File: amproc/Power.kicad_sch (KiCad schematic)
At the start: 42 parts

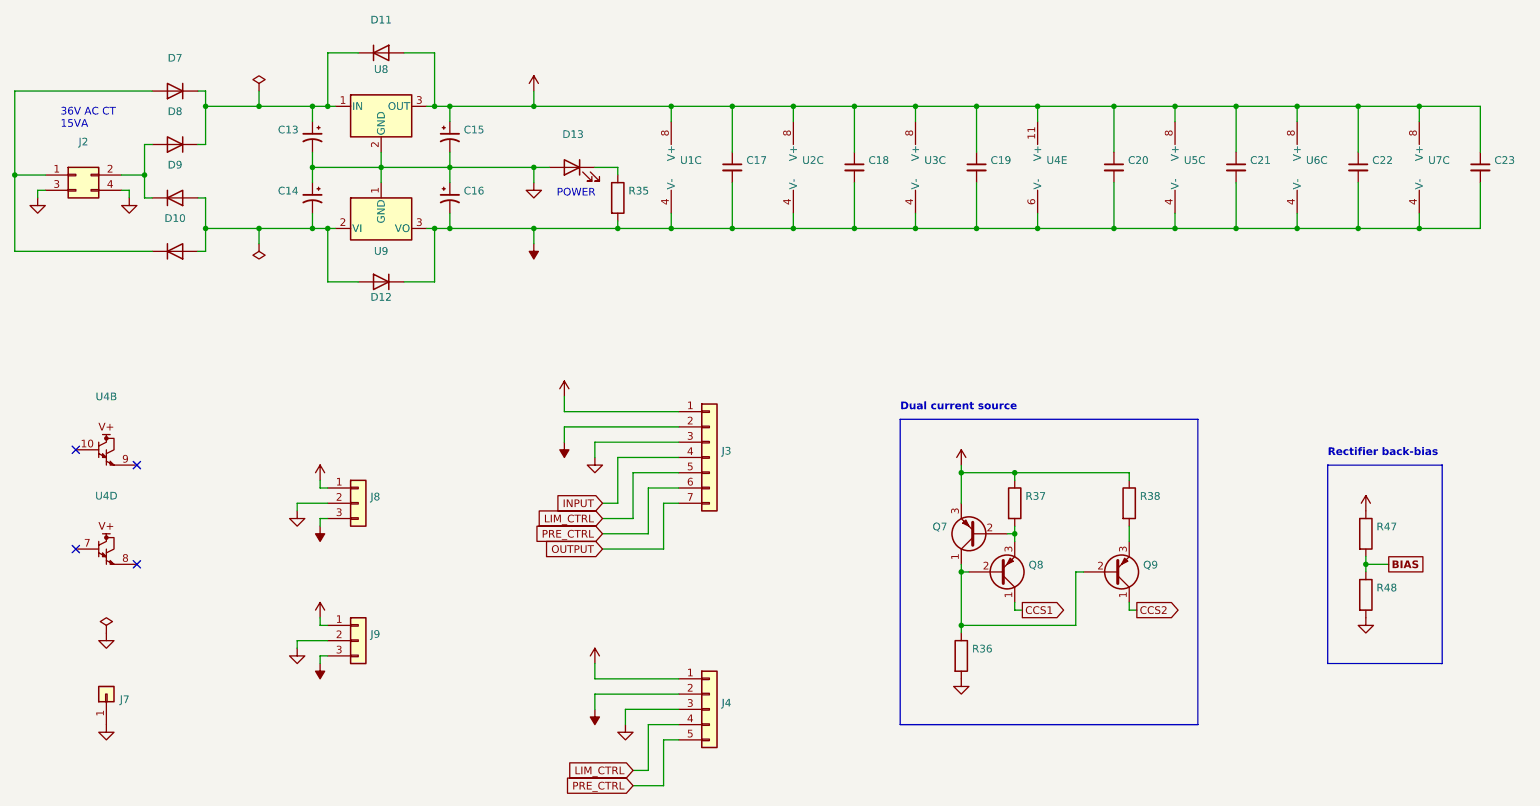
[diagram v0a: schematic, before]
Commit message: Fix U8, U9 pinouts
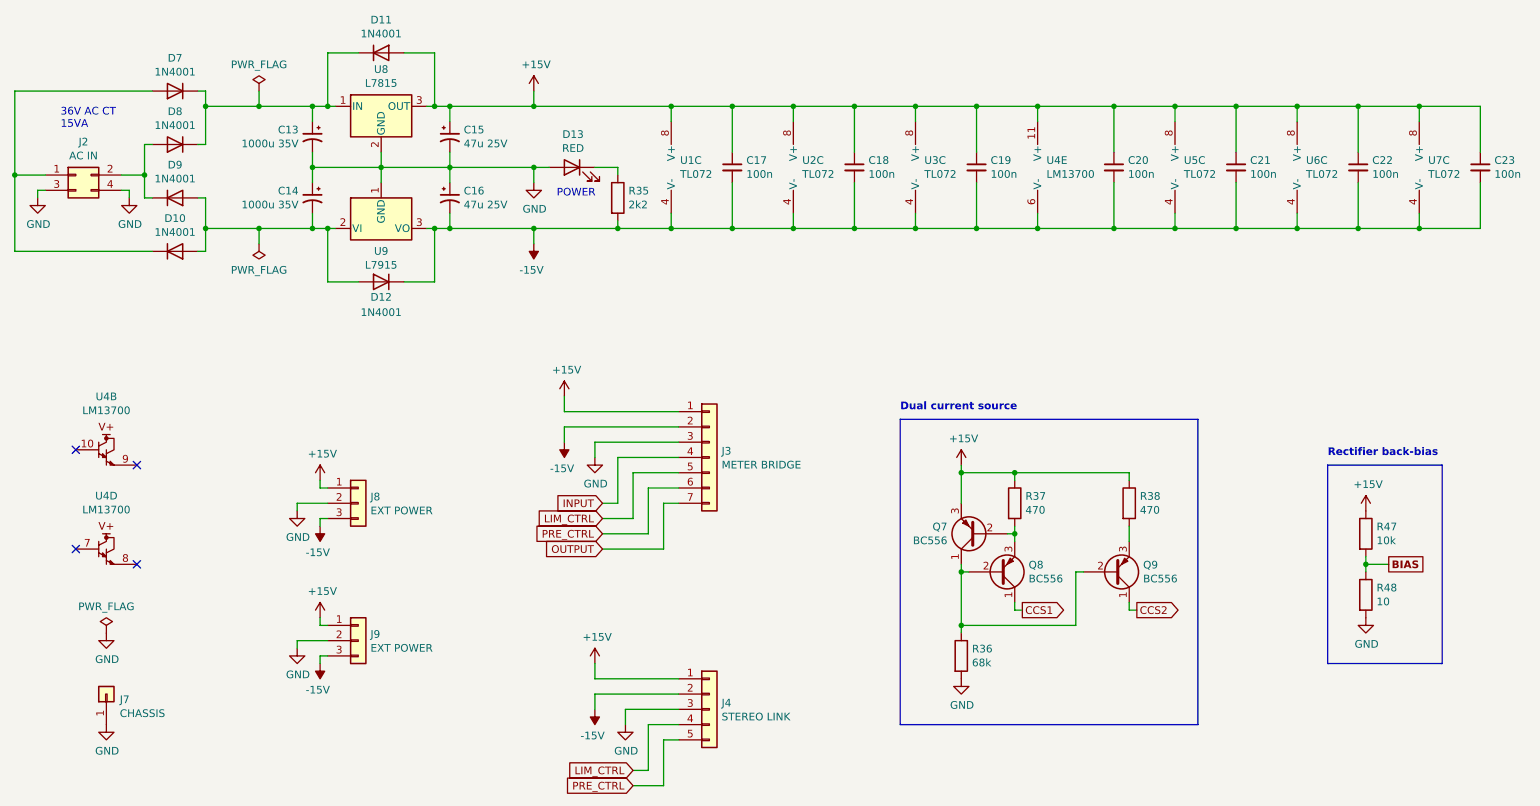
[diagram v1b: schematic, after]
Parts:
- C13, C14: value (none) -> 1000u 35V; footprint (none) -> Capacitors_THT:CP_Radial_D12.5mm_P5.00mm
- C15, C16: value (none) -> 47u 25V; footprint (none) -> Capacitors_THT:CP_Radial_D5.0mm_P2.00mm
- C17, C18, C19, C20, C21, C22, C23: value (none) -> 100n; footprint (none) -> Capacitors_THT:C_Disc_D4.7mm_W2.5mm_P5.00mm
- D10, D11, D12, D7, D8, D9: value (none) -> 1N4001; footprint (none) -> Diodes_THT:D_DO-41_SOD81_P10.16mm_Horizontal
- D13: value (none) -> RED; footprint (none) -> LEDs:LED_D5.0mm
- J2: value (none) -> AC IN; footprint (none) -> amproc:39-28-1043
- J3: value (none) -> METER BRIDGE; footprint (none) -> Connectors_JST:JST_XH_B07B-XH-A_07x2.50mm_Straight
- J4: value (none) -> STEREO LINK; footprint (none) -> Connectors_JST:JST_XH_B05B-XH-A_05x2.50mm_Straight
- J7: value (none) -> CHASSIS; footprint (none) -> amproc:TAB_378005.68
- J8, J9: value (none) -> EXT POWER; footprint (none) -> Connectors_JST:JST_XH_B03B-XH-A_03x2.50mm_Straight
- Q7, Q8, Q9: value (none) -> BC556; footprint (none) -> TO_SOT_Packages_THT:TO-92_Inline_Narrow_Oval
- R35: value (none) -> 2k2; footprint (none) -> amproc:R_Axial_DIN0207_L6.3mm_D2.5mm_P7.62mm_Horizontal_FabText
- R36: value (none) -> 68k; footprint (none) -> amproc:R_Axial_DIN0207_L6.3mm_D2.5mm_P7.62mm_Horizontal_FabText
- R37, R38: value (none) -> 470; footprint (none) -> amproc:R_Axial_DIN0207_L6.3mm_D2.5mm_P7.62mm_Horizontal_FabText
- R47: value (none) -> 10k; footprint (none) -> amproc:R_Axial_DIN0207_L6.3mm_D2.5mm_P7.62mm_Horizontal_FabText
- R48: value (none) -> 10; footprint (none) -> amproc:R_Axial_DIN0207_L6.3mm_D2.5mm_P7.62mm_Horizontal_FabText
- U1, U2, U3, U5, U6, U7: value (none) -> TL072; footprint (none) -> Housings_DIP:DIP-8_W7.62mm_LongPads
- U4: value (none) -> LM13700; footprint (none) -> Housings_DIP:DIP-16_W7.62mm_LongPads
- U8: value (none) -> L7815; footprint (none) -> Package_TO_SOT_THT:TO-220-3_Horizontal_TabUp
- U9: value (none) -> L7915; footprint (none) -> Package_TO_SOT_THT:TO-220-3_Horizontal_TabUp
